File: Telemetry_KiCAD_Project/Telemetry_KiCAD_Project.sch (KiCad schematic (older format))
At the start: 1 part

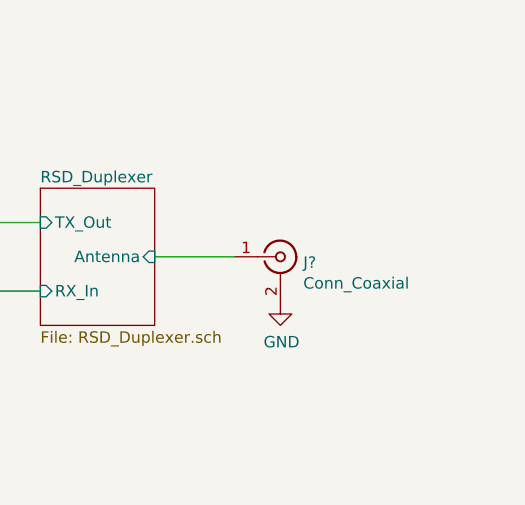
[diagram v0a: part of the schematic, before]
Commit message: Renamed Coax Connector Symbol
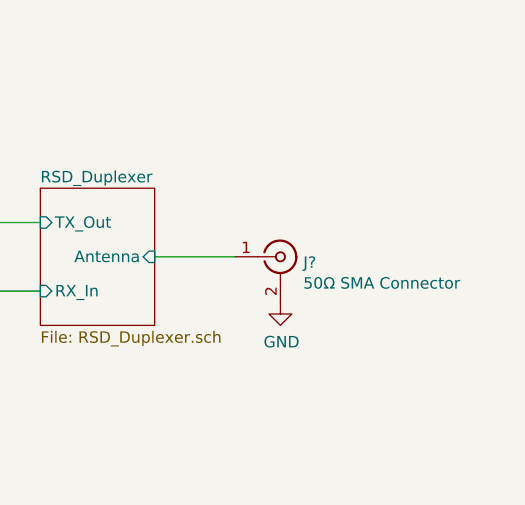
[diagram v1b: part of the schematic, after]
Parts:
- J?: value Conn_Coaxial -> 50Ω SMA Connector
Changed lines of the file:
@@
 P 8250 3450
 F 0 "J?" H 8350 3425 50  0000 L CNN
-F 1 "Conn_Coaxial" H 8350 3334 50  0000 L CNN
+F 1 "50Ω SMA Connector" H 8350 3334 50  0000 L CNN
 F 2 "" H 8250 3450 50  0001 C CNN
 F 3 " ~" H 8250 3450 50  0001 C CNN

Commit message: Added USB ESD, relocated Debug pins
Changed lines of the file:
@@
 $Descr A4 11693 8268
 encoding utf-8
-Sheet 1 7
+Sheet 1 8
 Title "Telemetry PCB Schematic"
 Date "2021-10-01"
@@
 F14 "SPI3_SCK" I R 2950 3150 50
 F15 "DEBUG_SWCLK" I L 1950 4100 50
-F16 "USB_DP" I R 2950 3650 50
-F17 "USB_DM" I R 2950 3500 50
+F16 "USB_DP" I R 2950 3950 50
+F17 "USB_DM" I R 2950 4100 50
 F18 "I2C1_EN" I L 1950 2250 50
 F19 "ABORT_1" I L 1950 3450 50
@@
 Wire Wire Line
 	2950 3150 3300 3150
+$Sheet
+S 4900 4550 500  400
+U 61A2ED84
+F0 "USB Connector and ESD" 50
+F1 "USB_ESD.sch" 50
+F2 "D-" I L 4900 4800 50
+F3 "D+" I L 4900 4650 50
+$EndSheet
+Wire Wire Line
+	4900 4650 3600 4650
+Wire Wire Line
+	3600 4650 3600 3950
+Wire Wire Line
+	3600 3950 2950 3950
+Wire Wire Line
+	2950 4100 3450 4100
+Wire Wire Line
+	3450 4100 3450 4800
+Wire Wire Line
+	3450 4800 4900 4800
 Wire Bus Line
 	3400 2300 3400 3050

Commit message: Correct SPI bus lines on main page
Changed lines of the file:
@@
 Text Label 3000 2700 0    50   ~ 0
 TX_SCL
+Text Label 3000 3150 0    50   ~ 0
+RX_SDO
 Text Label 3000 3000 0    50   ~ 0
-RX_SDO
-Text Label 3000 2850 0    50   ~ 0
 RX_SDI
-Text Label 3000 3150 0    50   ~ 0
+Text Label 3000 3300 0    50   ~ 0
 RX_SCL
 Entry Wire Line
@@
 	3300 2700 3400 2600
 Entry Wire Line
-	3300 2850 3400 2750
-Entry Wire Line
 	3300 3000 3400 2900
 Entry Wire Line
 	3300 3150 3400 3050
+Entry Wire Line
+	3300 3300 3400 3200
 $Sheet
 S 750  2100 500  2250
@@
 F10 "I2C1_SDA" I L 1950 2400 50
 F11 "I2C1_SCL" I L 1950 2550 50
-F12 "SPI3_MOSI" I R 2950 2850 50
-F13 "SPI3_MISO" I R 2950 3000 50
-F14 "SPI3_SCK" I R 2950 3150 50
+F12 "SPI3_MOSI" I R 2950 3000 50
+F13 "SPI3_MISO" I R 2950 3150 50
+F14 "SPI3_SCK" I R 2950 3300 50
 F15 "DEBUG_SWCLK" I L 1950 4100 50
 F16 "USB_DP" I R 2950 3950 50
@@
 F19 "ABORT_1" I L 1950 3450 50
 F20 "ABORT_2" I L 1950 3550 50
+F21 "EXT_INT1" I R 2950 2850 50
+F22 "EXT_INT2" I R 2950 3450 50
 $EndSheet
 Wire Wire Line
@@
 	3300 2700 2950 2700
 Wire Wire Line
-	2950 2850 3300 2850
+	2950 3000 3300 3000
 Wire Wire Line
-	3300 3000 2950 3000
+	3300 3150 2950 3150
 Wire Wire Line
-	2950 3150 3300 3150
+	2950 3300 3300 3300
 $Sheet
 S 4900 4550 500  400
@@
 Wire Wire Line
 	3450 4800 4900 4800
+Entry Wire Line
+	3300 2850 3400 2750
+Entry Wire Line
+	3300 3450 3400 3350
+Wire Wire Line
+	3300 3450 2950 3450
+Wire Wire Line
+	2950 2850 3300 2850
+Text Label 3000 2850 0    50   ~ 0
+TX_IRQ
+Text Label 3000 3450 0    50   ~ 0
+RX_IRQ
+Entry Wire Line
+	4400 2400 4500 2500
+Entry Wire Line
+	4400 3550 4500 3650
+Wire Wire Line
+	4500 2500 4900 2500
+Wire Wire Line
+	4900 3650 4500 3650
 Wire Bus Line
-	3400 2300 3400 3050
+	3400 2300 3400 3350
 Wire Bus Line
 	4400 2300 4400 4000
+Text Label 4550 2500 0    50   ~ 0
+TX_IRQ
+Text Label 4550 3650 0    50   ~ 0
+RX_IRQ
 $EndSCHEMATC

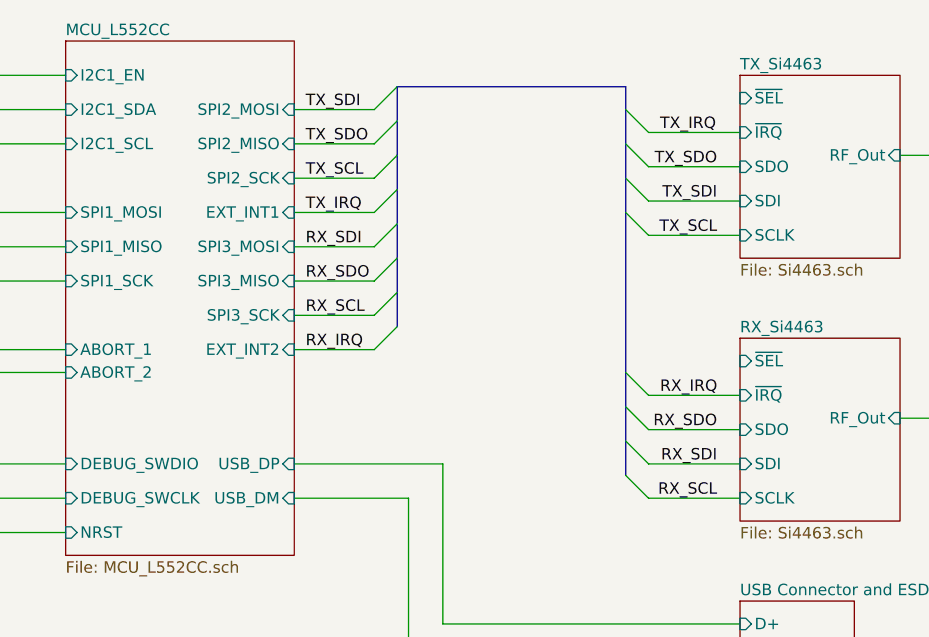
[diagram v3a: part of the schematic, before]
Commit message: Added chip select functions for RX and TX chips
The Si4463 datasheet mentions that some parameters can be quickly accessed if the chip select line is toggled
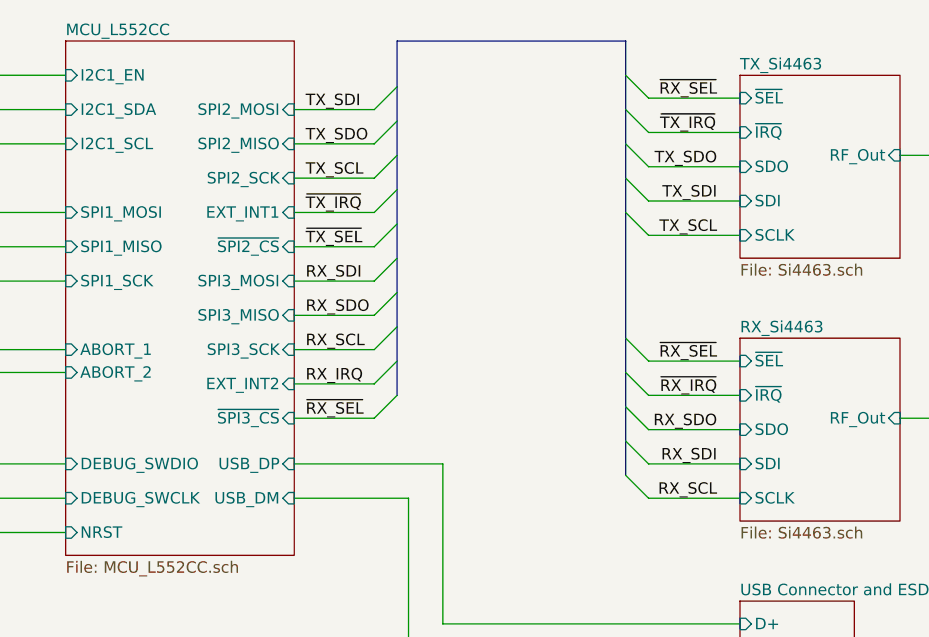
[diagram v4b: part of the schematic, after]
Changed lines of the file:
@@
 Text Label 3000 2700 0    50   ~ 0
 TX_SCL
+Text Label 3000 3300 0    50   ~ 0
+RX_SDO
 Text Label 3000 3150 0    50   ~ 0
-RX_SDO
-Text Label 3000 3000 0    50   ~ 0
 RX_SDI
-Text Label 3000 3300 0    50   ~ 0
+Text Label 3000 3450 0    50   ~ 0
 RX_SCL
 Entry Wire Line
@@
 	3300 2700 3400 2600
 Entry Wire Line
-	3300 3000 3400 2900
-Entry Wire Line
 	3300 3150 3400 3050
 Entry Wire Line
 	3300 3300 3400 3200
+Entry Wire Line
+	3300 3450 3400 3350
 $Sheet
 S 750  2100 500  2250
@@
 Wire Wire Line
 	1250 2250 1950 2250
-Wire Bus Line
-	3400 2300 4400 2300
 $Sheet
 S 1950 2100 1000 2250
@@
 F10 "I2C1_SDA" I L 1950 2400 50
 F11 "I2C1_SCL" I L 1950 2550 50
-F12 "SPI3_MOSI" I R 2950 3000 50
-F13 "SPI3_MISO" I R 2950 3150 50
-F14 "SPI3_SCK" I R 2950 3300 50
+F12 "SPI3_MOSI" I R 2950 3150 50
+F13 "SPI3_MISO" I R 2950 3300 50
+F14 "SPI3_SCK" I R 2950 3450 50
 F15 "DEBUG_SWCLK" I L 1950 4100 50
 F16 "USB_DP" I R 2950 3950 50
@@
 F20 "ABORT_2" I L 1950 3550 50
 F21 "EXT_INT1" I R 2950 2850 50
-F22 "EXT_INT2" I R 2950 3450 50
+F22 "EXT_INT2" I R 2950 3600 50
+F23 "~SPI2_CS" I R 2950 3000 50
+F24 "~SPI3_CS" I R 2950 3750 50
 $EndSheet
 Wire Wire Line
@@
 	3300 2700 2950 2700
 Wire Wire Line
-	2950 3000 3300 3000
+	2950 3150 3300 3150
 Wire Wire Line
-	3300 3150 2950 3150
+	3300 3300 2950 3300
 Wire Wire Line
-	2950 3300 3300 3300
+	2950 3450 3300 3450
 $Sheet
 S 4900 4550 500  400
@@
 	3300 2850 3400 2750
 Entry Wire Line
-	3300 3450 3400 3350
+	3300 3600 3400 3500
 Wire Wire Line
-	3300 3450 2950 3450
+	3300 3600 2950 3600
 Wire Wire Line
 	2950 2850 3300 2850
 Text Label 3000 2850 0    50   ~ 0
-TX_IRQ
-Text Label 3000 3450 0    50   ~ 0
+~TX_IRQ
+Text Label 3000 3600 0    50   ~ 0
 RX_IRQ
 Entry Wire Line
@@
 Wire Wire Line
 	4900 3650 4500 3650
+Text Label 4550 2500 0    50   ~ 0
+~TX_IRQ
+Text Label 4800 3650 2    50   ~ 0
+~RX_IRQ
+Entry Wire Line
+	3300 3750 3400 3650
+Entry Wire Line
+	3300 3000 3400 2900
+Wire Wire Line
+	2950 3000 3300 3000
+Wire Wire Line
+	2950 3750 3300 3750
+Text Label 3000 3000 0    50   ~ 0
+~TX_SEL
 Wire Bus Line
-	3400 2300 3400 3350
+	4400 2100 3400 2100
+Entry Wire Line
+	4400 2250 4500 2350
+Wire Wire Line
+	4500 2350 4900 2350
+Text Label 3000 3750 0    50   ~ 0
+~RX_SEL
+Text Label 4800 2350 2    50   ~ 0
+~RX_SEL
+Entry Wire Line
+	4400 3400 4500 3500
+Wire Wire Line
+	4500 3500 4900 3500
 Wire Bus Line
-	4400 2300 4400 4000
-Text Label 4550 2500 0    50   ~ 0
-TX_IRQ
-Text Label 4550 3650 0    50   ~ 0
-RX_IRQ
+	4400 2100 4400 4000
+Wire Bus Line
+	3400 2100 3400 3650
+Text Label 4800 3500 2    50   ~ 0
+~RX_SEL
 $EndSCHEMATC

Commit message: Annotated Components
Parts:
- gave numbers to parts that had none: 1
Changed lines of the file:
@@
 $EndSheet
 $Comp
-L Connector:Conn_Coaxial J?
+L Connector:Conn_Coaxial J1
 U 1 1 619FD788
 P 8250 3450
-F 0 "J?" H 8350 3425 50  0000 L CNN
+F 0 "J1" H 8350 3425 50  0000 L CNN
 F 1 "50Ω SMA Connector" H 8350 3334 50  0000 L CNN
 F 2 "" H 8250 3450 50  0001 C CNN
@@
 $EndComp
 $Comp
-L power:GND #PWR?
+L power:GND #PWR0101
 U 1 1 619FE4AD
 P 8250 3650
-F 0 "#PWR?" H 8250 3400 50  0001 C CNN
+F 0 "#PWR0101" H 8250 3400 50  0001 C CNN
 F 1 "GND" H 8255 3477 50  0000 C CNN
 F 2 "" H 8250 3650 50  0001 C CNN

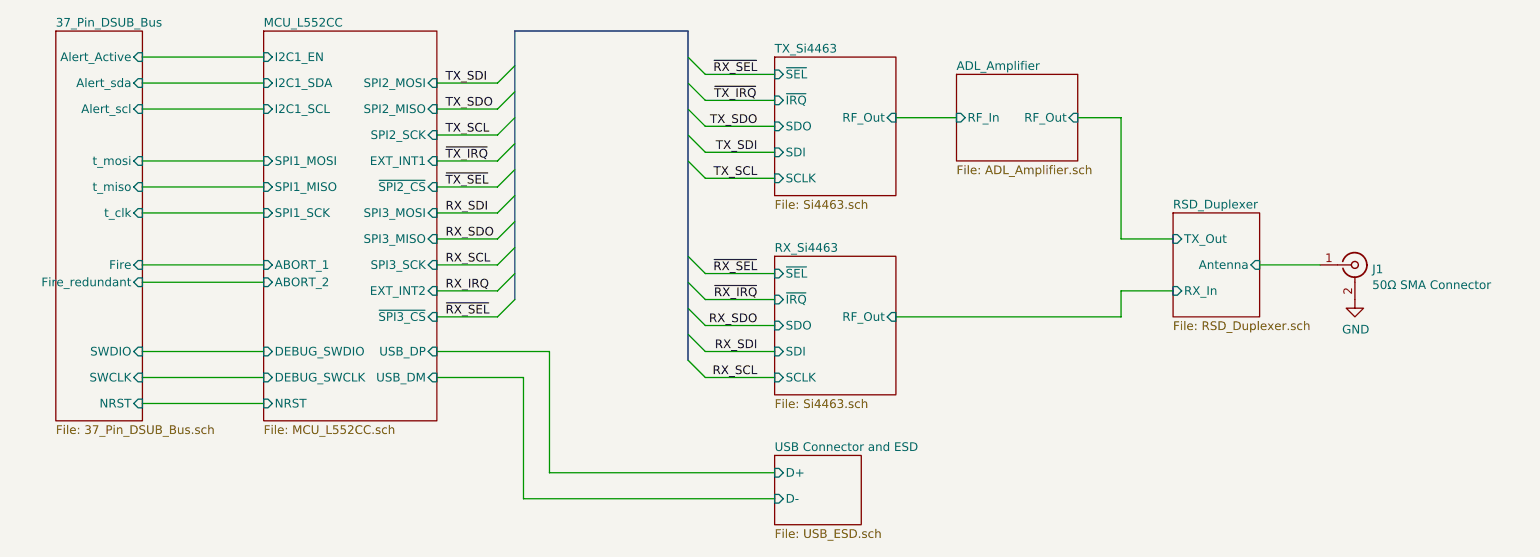
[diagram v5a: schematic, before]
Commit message: Corrected hierarchical pin directions, squashed bugs
There are still some warnings about pins being connected but not driven, don't know how to fix those at the moment
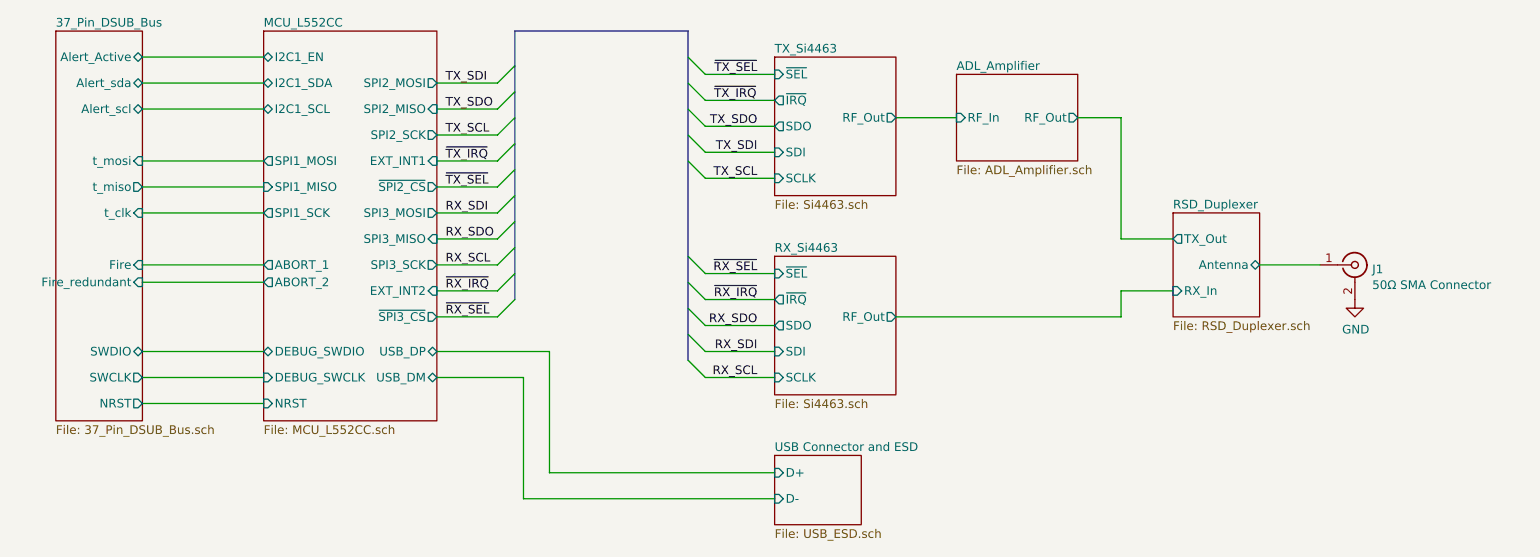
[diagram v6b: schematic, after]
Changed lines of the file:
@@
 F0 "RSD_Duplexer" 50
 F1 "RSD_Duplexer.sch" 50
-F2 "TX_Out" I L 7200 3300 50
-F3 "RX_In" I L 7200 3600 50
-F4 "Antenna" I R 7700 3450 50
+F2 "RX_In" I L 7200 3600 50
+F3 "TX_Out" O L 7200 3300 50
+F4 "Antenna" B R 7700 3450 50
 $EndSheet
 $Comp
@@
 F1 "Si4463.sch" 50
 F2 "~SEL" I L 4900 2350 50
-F3 "~IRQ" I L 4900 2500 50
-F4 "SDO" I L 4900 2650 50
-F5 "SDI" I L 4900 2800 50
-F6 "SCLK" I L 4900 2950 50
-F7 "RF_Out" I R 5600 2600 50
+F3 "SDI" I L 4900 2800 50
+F4 "SCLK" I L 4900 2950 50
+F5 "~IRQ" O L 4900 2500 50
+F6 "SDO" O L 4900 2650 50
+F7 "RF_Out" O R 5600 2600 50
 $EndSheet
 $Sheet
@@
 F1 "ADL_Amplifier.sch" 50
 F2 "RF_In" I L 5950 2600 50
-F3 "RF_Out" I R 6650 2600 50
+F3 "RF_Out" O R 6650 2600 50
 $EndSheet
 $Sheet
@@
 F1 "Si4463.sch" 50
 F2 "~SEL" I L 4900 3500 50
-F3 "~IRQ" I L 4900 3650 50
-F4 "SDO" I L 4900 3800 50
-F5 "SDI" I L 4900 3950 50
-F6 "SCLK" I L 4900 4100 50
-F7 "RF_Out" I R 5600 3750 50
+F3 "SDI" I L 4900 3950 50
+F4 "SCLK" I L 4900 4100 50
+F5 "~IRQ" O L 4900 3650 50
+F6 "SDO" O L 4900 3800 50
+F7 "RF_Out" O R 5600 3750 50
 $EndSheet
 Wire Wire Line
@@
 Entry Wire Line
 	3300 3450 3400 3350
-$Sheet
-S 750  2100 500  2250
-U 619DC150
-F0 "37_Pin_DSUB_Bus" 50
-F1 "37_Pin_DSUB_Bus.sch" 50
-F2 "t_mosi" I R 1250 2850 50
-F3 "t_miso" I R 1250 3000 50
-F4 "t_clk" I R 1250 3150 50
-F5 "Alert_scl" I R 1250 2550 50
-F6 "Alert_sda" I R 1250 2400 50
-F7 "Alert_Active" I R 1250 2250 50
-F8 "SWDIO" I R 1250 3950 50
-F9 "SWCLK" I R 1250 4100 50
-F10 "NRST" I R 1250 4250 50
-F11 "Fire" I R 1250 3450 50
-F12 "Fire_redundant" I R 1250 3550 50
-$EndSheet
 Wire Wire Line
 	1250 4250 1950 4250
@@
 Wire Wire Line
 	1250 2250 1950 2250
-$Sheet
-S 1950 2100 1000 2250
-U 619FB6DF
-F0 "MCU_L552CC" 50
-F1 "MCU_L552CC.sch" 50
-F2 "NRST" I L 1950 4250 50
-F3 "SPI1_SCK" I L 1950 3150 50
-F4 "SPI1_MISO" I L 1950 3000 50
-F5 "SPI1_MOSI" I L 1950 2850 50
-F6 "SPI2_SCK" I R 2950 2700 50
-F7 "SPI2_MISO" I R 2950 2550 50
-F8 "SPI2_MOSI" I R 2950 2400 50
-F9 "DEBUG_SWDIO" I L 1950 3950 50
-F10 "I2C1_SDA" I L 1950 2400 50
-F11 "I2C1_SCL" I L 1950 2550 50
-F12 "SPI3_MOSI" I R 2950 3150 50
-F13 "SPI3_MISO" I R 2950 3300 50
-F14 "SPI3_SCK" I R 2950 3450 50
-F15 "DEBUG_SWCLK" I L 1950 4100 50
-F16 "USB_DP" I R 2950 3950 50
-F17 "USB_DM" I R 2950 4100 50
-F18 "I2C1_EN" I L 1950 2250 50
-F19 "ABORT_1" I L 1950 3450 50
-F20 "ABORT_2" I L 1950 3550 50
-F21 "EXT_INT1" I R 2950 2850 50
-F22 "EXT_INT2" I R 2950 3600 50
-F23 "~SPI2_CS" I R 2950 3000 50
-F24 "~SPI3_CS" I R 2950 3750 50
-$EndSheet
 Wire Wire Line
 	3300 2400 2950 2400
@@
 ~TX_IRQ
 Text Label 3000 3600 0    50   ~ 0
-RX_IRQ
+~RX_IRQ
 Entry Wire Line
 	4400 2400 4500 2500
@@
 ~RX_SEL
 Text Label 4800 2350 2    50   ~ 0
+~TX_SEL
+Entry Wire Line
+	4400 3400 4500 3500
+Wire Wire Line
+	4500 3500 4900 3500
+Text Label 4800 3500 2    50   ~ 0
 ~RX_SEL
-Entry Wire Line
-	4400 3400 4500 3500
-Wire Wire Line
-	4500 3500 4900 3500
 Wire Bus Line
 	4400 2100 4400 4000
 Wire Bus Line
 	3400 2100 3400 3650
-Text Label 4800 3500 2    50   ~ 0
-~RX_SEL
+$Sheet
+S 1950 2100 1000 2250
+U 619FB6DF
+F0 "MCU_L552CC" 50
+F1 "MCU_L552CC.sch" 50
+F2 "NRST" I L 1950 4250 50
+F3 "SPI1_MISO" I L 1950 3000 50
+F4 "SPI2_MISO" I R 2950 2550 50
+F5 "SPI3_MISO" I R 2950 3300 50
+F6 "EXT_INT1" I R 2950 2850 50
+F7 "EXT_INT2" I R 2950 3600 50
+F8 "I2C1_EN" B L 1950 2250 50
+F9 "SPI1_MOSI" O L 1950 2850 50
+F10 "SPI1_SCK" O L 1950 3150 50
+F11 "ABORT_2" O L 1950 3550 50
+F12 "ABORT_1" O L 1950 3450 50
+F13 "DEBUG_SWDIO" B L 1950 3950 50
+F14 "DEBUG_SWCLK" I L 1950 4100 50
+F15 "SPI2_MOSI" O R 2950 2400 50
+F16 "SPI2_SCK" O R 2950 2700 50
+F17 "~SPI2_CS" O R 2950 3000 50
+F18 "SPI3_MOSI" O R 2950 3150 50
+F19 "SPI3_SCK" O R 2950 3450 50
+F20 "~SPI3_CS" O R 2950 3750 50
+F21 "USB_DP" B R 2950 3950 50
+F22 "USB_DM" B R 2950 4100 50
+F23 "I2C1_SDA" B L 1950 2400 50
+F24 "I2C1_SCL" B L 1950 2550 50
+$EndSheet
+$Sheet
+S 750  2100 500  2250
+U 619DC150
+F0 "37_Pin_DSUB_Bus" 50
+F1 "37_Pin_DSUB_Bus.sch" 50
+F2 "t_mosi" I R 1250 2850 50
+F3 "t_clk" I R 1250 3150 50
+F4 "Fire" I R 1250 3450 50
+F5 "Fire_redundant" I R 1250 3550 50
+F6 "Alert_Active" B R 1250 2250 50
+F7 "Alert_scl" B R 1250 2550 50
+F8 "Alert_sda" B R 1250 2400 50
+F9 "t_miso" O R 1250 3000 50
+F10 "SWDIO" B R 1250 3950 50
+F11 "SWCLK" O R 1250 4100 50
+F12 "NRST" O R 1250 4250 50
+$EndSheet
 $EndSCHEMATC

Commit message: Assigned footprints to all components (except duplexer)
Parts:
- J1: footprint (none) -> Connector_Coaxial:SMA_Amphenol_132134-11_Vertical
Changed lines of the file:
@@
 F 0 "J1" H 8350 3425 50  0000 L CNN
 F 1 "50Ω SMA Connector" H 8350 3334 50  0000 L CNN
-F 2 "" H 8250 3450 50  0001 C CNN
+F 2 "Connector_Coaxial:SMA_Amphenol_132134-11_Vertical" H 8250 3450 50  0001 C CNN
 F 3 " ~" H 8250 3450 50  0001 C CNN
 	1    8250 3450
